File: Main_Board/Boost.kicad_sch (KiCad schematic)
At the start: 13 parts, among them U3 TLV61070ADBV

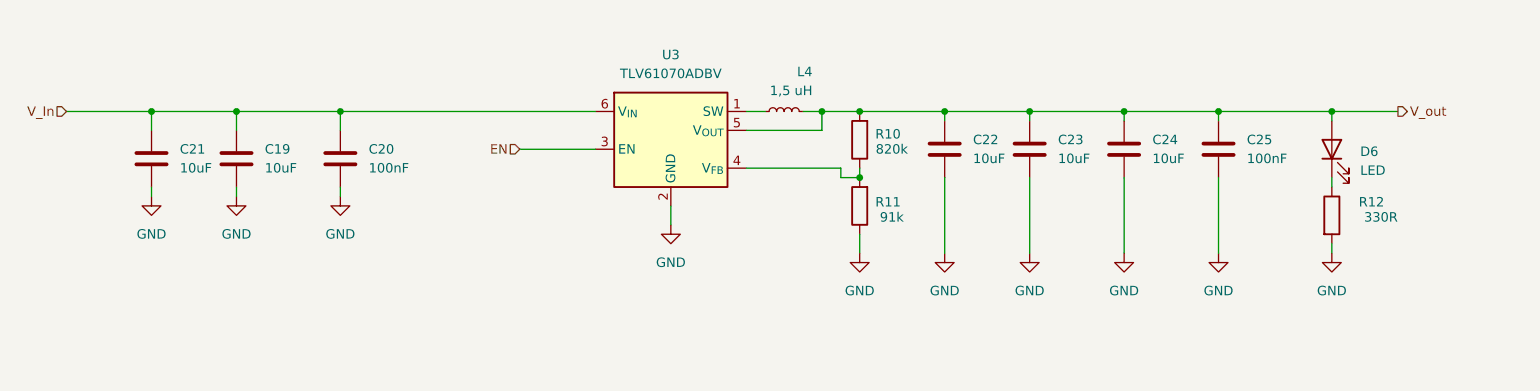
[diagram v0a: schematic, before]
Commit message: Input Protection
Irlm is left to be calculated
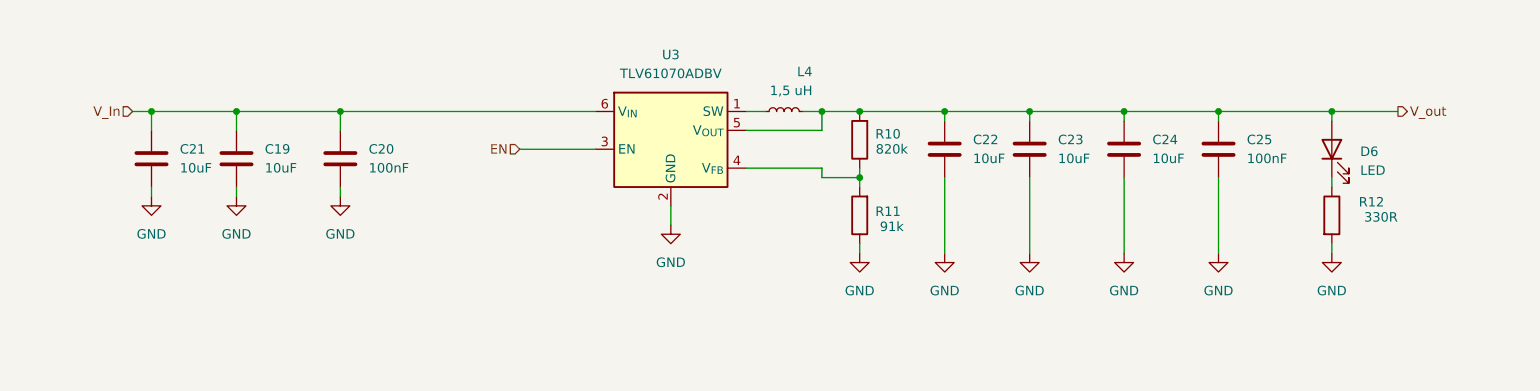
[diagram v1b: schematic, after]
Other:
- moved on the sheet: R11
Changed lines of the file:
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@@
 	(wire
 		(pts
-			(xy 134.62 93.98) (xy 147.32 93.98)
-		)
-		(stroke
-			(width 0)
-			(type default)
-		)
-	)
-	(wire
-		(pts
-			(xy 149.86 102.87) (xy 149.86 105.41)
+			(xy 134.62 93.98) (xy 144.78 93.98)
+		)
+		(stroke
+			(width 0)
+			(type default)
+		)
+	)
+	(wire
+		(pts
+			(xy 149.86 104.14) (xy 149.86 105.41)
 		)
 		(stroke
@@
 	(wire
 		(pts
+			(xy 149.86 96.52) (xy 149.86 95.25)
+		)
+		(stroke
+			(width 0)
+			(type default)
+		)
+	)
+	(wire
+		(pts
 			(xy 161.29 87.63) (xy 161.29 86.36)
 		)
@@
 	(wire
 		(pts
-			(xy 43.18 86.36) (xy 54.61 86.36)
+			(xy 52.07 86.36) (xy 54.61 86.36)
 		)
 		(stroke
@@
 	(wire
 		(pts
-			(xy 147.32 93.98) (xy 147.32 95.25)
+			(xy 144.78 93.98) (xy 144.78 95.25)
 		)
 		(stroke
@@
 	(wire
 		(pts
-			(xy 147.32 95.25) (xy 149.86 95.25)
+			(xy 144.78 95.25) (xy 149.86 95.25)
 		)
 		(stroke
@@
 		)
 	)
-	(hierarchical_label "V_In"
+	(hierarchical_label "EN"
 		(shape input)
-		(at 43.18 86.36 180)
+		(at 104.14 91.44 180)
 		(effects
 			(font
@@
 		)
 	)
-	(hierarchical_label "EN"
+	(hierarchical_label "V_In"
 		(shape input)
-		(at 104.14 91.44 180)
+		(at 52.07 86.36 180)
 		(effects
 			(font
@@
 	(symbol
 		(lib_id "Device:R")
-		(at 149.86 99.06 180)
+		(at 149.86 100.33 180)
 		(unit 1)
 		(body_style 1)
@@
 		(dnp no)
 		(property "Reference" "R11"
-			(at 153.67 98.552 0)
+			(at 153.67 99.822 0)
 			(show_name no)
 			(do_not_autoplace no)
@@
 		)
 		(property "Value" "91k"
-			(at 154.178 100.584 0)
+			(at 154.178 101.854 0)
 			(show_name no)
 			(do_not_autoplace no)
@@
 		)
 		(property "Footprint" ""
-			(at 151.638 99.06 90)
+			(at 151.638 100.33 90)
 			(hide yes)
 			(show_name no)
@@
 		)
 		(property "Datasheet" ""
-			(at 149.86 99.06 0)
+			(at 149.86 100.33 0)
 			(hide yes)
 			(show_name no)
@@
 		)
 		(property "Description" "Resistor"
-			(at 149.86 99.06 0)
-			(hide yes)
-			(show_name no)
+			(at 149.86 100.33 0)
+			(hide yes)
+			(show_name no)

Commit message: Add buzzer, Add LED, ADD R&D jumper
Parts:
- renumbered C21 to C20, C19 to C21, C20 to C22, C22 to C23, C23 to C24, C24 to C25, C25 to C26, L4 to L3, R10 to R25, R11 to R26, R12 to R27, U3 to U5
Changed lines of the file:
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@@
 		(dnp no)
 		(fields_autoplaced yes)
-		(property "Reference" "#PWR052"
+		(property "Reference" "#PWR055"
 			(at 149.86 111.76 0)
 			(hide yes)
@@
 			(project "Main_Board"
 				(path "/7481738f-7c20-40bb-99b0-6ccd4168db33/4704f5be-58a0-4191-b01f-84980581c4a3/0e0beba8-65f6-4fdb-a51c-805313830f65"
-					(reference "#PWR052")
+					(reference "#PWR055")
 					(unit 1)
 				)
@@
 		(in_pos_files yes)
 		(dnp no)
-		(property "Reference" "R11"
+		(property "Reference" "R26"
 			(at 153.67 99.822 0)
 			(show_name no)
@@
 			(project "Main_Board"
 				(path "/7481738f-7c20-40bb-99b0-6ccd4168db33/4704f5be-58a0-4191-b01f-84980581c4a3/0e0beba8-65f6-4fdb-a51c-805313830f65"
-					(reference "R11")
+					(reference "R26")
 					(unit 1)
 				)
@@
 		(dnp no)
 		(fields_autoplaced yes)
-		(property "Reference" "#PWR053"
+		(property "Reference" "#PWR060"
 			(at 213.36 111.76 0)
 			(hide yes)
@@
 			(project "Main_Board"
 				(path "/7481738f-7c20-40bb-99b0-6ccd4168db33/4704f5be-58a0-4191-b01f-84980581c4a3/0e0beba8-65f6-4fdb-a51c-805313830f65"
-					(reference "#PWR053")
+					(reference "#PWR060")
 					(unit 1)
 				)
@@
 		(dnp no)
 		(fields_autoplaced yes)
-		(property "Reference" "C20"
+		(property "Reference" "C22"
 			(at 83.82 91.4399 0)
 			(show_name no)
@@
 			(project "Main_Board"
 				(path "/7481738f-7c20-40bb-99b0-6ccd4168db33/4704f5be-58a0-4191-b01f-84980581c4a3/0e0beba8-65f6-4fdb-a51c-805313830f65"
-					(reference "C20")
+					(reference "C22")
 					(unit 1)
 				)
@@
 		(dnp no)
 		(fields_autoplaced yes)
-		(property "Reference" "U3"
+		(property "Reference" "U5"
 			(at 124.46 78.74 0)
 			(show_name no)
@@
 			(project "Main_Board"
 				(path "/7481738f-7c20-40bb-99b0-6ccd4168db33/4704f5be-58a0-4191-b01f-84980581c4a3/0e0beba8-65f6-4fdb-a51c-805313830f65"
-					(reference "U3")
+					(reference "U5")
 					(unit 1)
 				)
@@
 		(dnp no)
 		(fields_autoplaced yes)
-		(property "Reference" "C22"
+		(property "Reference" "C23"
 			(at 165.1 90.1699 0)
 			(show_name no)
@@
 			(project "Main_Board"
 				(path "/7481738f-7c20-40bb-99b0-6ccd4168db33/4704f5be-58a0-4191-b01f-84980581c4a3/0e0beba8-65f6-4fdb-a51c-805313830f65"
-					(reference "C22")
+					(reference "C23")
 					(unit 1)
 				)
@@
 		(in_pos_files yes)
 		(dnp no)
-		(property "Reference" "L4"
+		(property "Reference" "L3"
 			(at 143.51 81.026 90)
 			(show_name no)
@@
 			(project "Main_Board"
 				(path "/7481738f-7c20-40bb-99b0-6ccd4168db33/4704f5be-58a0-4191-b01f-84980581c4a3/0e0beba8-65f6-4fdb-a51c-805313830f65"
-					(reference "L4")
+					(reference "L3")
 					(unit 1)
 				)
@@
 		(dnp no)
 		(fields_autoplaced yes)
-		(property "Reference" "#PWR048"
+		(property "Reference" "#PWR056"
 			(at 161.29 111.76 0)
 			(hide yes)
@@
 			(project "Main_Board"
 				(path "/7481738f-7c20-40bb-99b0-6ccd4168db33/4704f5be-58a0-4191-b01f-84980581c4a3/0e0beba8-65f6-4fdb-a51c-805313830f65"
-					(reference "#PWR048")
+					(reference "#PWR056")
 					(unit 1)
 				)
@@
 		(dnp no)
 		(fields_autoplaced yes)
-		(property "Reference" "#PWR044"
+		(property "Reference" "#PWR052"
 			(at 66.04 104.14 0)
 			(hide yes)
@@
 			(project "Main_Board"
 				(path "/7481738f-7c20-40bb-99b0-6ccd4168db33/4704f5be-58a0-4191-b01f-84980581c4a3/0e0beba8-65f6-4fdb-a51c-805313830f65"
-					(reference "#PWR044")
+					(reference "#PWR052")
 					(unit 1)
 				)
@@
 		(dnp no)
 		(fields_autoplaced yes)
-		(property "Reference" "C25"
+		(property "Reference" "C26"
 			(at 201.93 90.1699 0)
 			(show_name no)
@@
 			(project "Main_Board"
 				(path "/7481738f-7c20-40bb-99b0-6ccd4168db33/4704f5be-58a0-4191-b01f-84980581c4a3/0e0beba8-65f6-4fdb-a51c-805313830f65"
-					(reference "C25")
+					(reference "C26")
 					(unit 1)
 				)
@@
 		(dnp no)
 		(fields_autoplaced yes)
-		(property "Reference" "C21"
+		(property "Reference" "C20"
 			(at 58.42 91.4399 0)
 			(show_name no)
@@
 			(project "Main_Board"
 				(path "/7481738f-7c20-40bb-99b0-6ccd4168db33/4704f5be-58a0-4191-b01f-84980581c4a3/0e0beba8-65f6-4fdb-a51c-805313830f65"
-					(reference "C21")
+					(reference "C20")
 					(unit 1)
 				)
@@
 		(dnp no)
 		(fields_autoplaced yes)
-		(property "Reference" "#PWR047"
+		(property "Reference" "#PWR054"
 			(at 124.46 107.95 0)
 			(hide yes)
@@
 			(project "Main_Board"
 				(path "/7481738f-7c20-40bb-99b0-6ccd4168db33/4704f5be-58a0-4191-b01f-84980581c4a3/0e0beba8-65f6-4fdb-a51c-805313830f65"
-					(reference "#PWR047")
+					(reference "#PWR054")
 					(unit 1)
 				)
@@
 		(dnp no)
 		(fields_autoplaced yes)
-		(property "Reference" "#PWR049"
+		(property "Reference" "#PWR057"
 			(at 172.72 111.76 0)
 			(hide yes)
@@
 			(project "Main_Board"
 				(path "/7481738f-7c20-40bb-99b0-6ccd4168db33/4704f5be-58a0-4191-b01f-84980581c4a3/0e0beba8-65f6-4fdb-a51c-805313830f65"
-					(reference "#PWR049")
+					(reference "#PWR057")
 					(unit 1)
 				)
@@
 		(dnp no)
 		(fields_autoplaced yes)
-		(property "Reference" "#PWR045"
+		(property "Reference" "#PWR053"
 			(at 80.01 104.14 0)
 			(hide yes)
@@
 			(project "Main_Board"
 				(path "/7481738f-7c20-40bb-99b0-6ccd4168db33/4704f5be-58a0-4191-b01f-84980581c4a3/0e0beba8-65f6-4fdb-a51c-805313830f65"
-					(reference "#PWR045")
+					(reference "#PWR053")
 					(unit 1)
 				)
@@
 		(dnp no)
 		(fields_autoplaced yes)
-		(property "Reference" "C19"
+		(property "Reference" "C21"
 			(at 69.85 91.4399 0)
 			(show_name no)
@@
 			(project "Main_Board"
 				(path "/7481738f-7c20-40bb-99b0-6ccd4168db33/4704f5be-58a0-4191-b01f-84980581c4a3/0e0beba8-65f6-4fdb-a51c-805313830f65"
-					(reference "C19")
+					(reference "C21")
 					(unit 1)
 				)
@@
 		(dnp no)
 		(fields_autoplaced yes)
-		(property "Reference" "#PWR046"
+		(property "Reference" "#PWR051"
 			(at 54.61 104.14 0)
 			(hide yes)
@@
 			(project "Main_Board"
 				(path "/7481738f-7c20-40bb-99b0-6ccd4168db33/4704f5be-58a0-4191-b01f-84980581c4a3/0e0beba8-65f6-4fdb-a51c-805313830f65"
-					(reference "#PWR046")
+					(reference "#PWR051")
 					(unit 1)
 				)
@@
 		(dnp no)
 		(fields_autoplaced yes)
-		(property "Reference" "#PWR050"
+		(property "Reference" "#PWR058"
 			(at 185.42 111.76 0)
 			(hide yes)
@@
 			(project "Main_Board"
 				(path "/7481738f-7c20-40bb-99b0-6ccd4168db33/4704f5be-58a0-4191-b01f-84980581c4a3/0e0beba8-65f6-4fdb-a51c-805313830f65"
-					(reference "#PWR050")
+					(reference "#PWR058")
 					(unit 1)
 				)
@@
 		(dnp no)
 		(fields_autoplaced yes)
-		(property "Reference" "C23"
+		(property "Reference" "C24"
 			(at 176.53 90.1699 0)
 			(show_name no)
@@
 			(project "Main_Board"
 				(path "/7481738f-7c20-40bb-99b0-6ccd4168db33/4704f5be-58a0-4191-b01f-84980581c4a3/0e0beba8-65f6-4fdb-a51c-805313830f65"
-					(reference "C23")
+					(reference "C24")
 					(unit 1)
 				)
@@
 		(dnp no)
 		(fields_autoplaced yes)
-		(property "Reference" "#PWR051"
+		(property "Reference" "#PWR059"
 			(at 198.12 111.76 0)
 			(hide yes)
@@
 			(project "Main_Board"
 				(path "/7481738f-7c20-40bb-99b0-6ccd4168db33/4704f5be-58a0-4191-b01f-84980581c4a3/0e0beba8-65f6-4fdb-a51c-805313830f65"
-					(reference "#PWR051")
+					(reference "#PWR059")
 					(unit 1)
 				)
@@
 		(in_pos_files yes)
 		(dnp no)
-		(property "Reference" "R12"
+		(property "Reference" "R27"
 			(at 218.694 98.552 0)
 			(show_name no)
@@
 			(project "Main_Board"
 				(path "/7481738f-7c20-40bb-99b0-6ccd4168db33/4704f5be-58a0-4191-b01f-84980581c4a3/0e0beba8-65f6-4fdb-a51c-805313830f65"
-					(reference "R12")
+					(reference "R27")
 					(unit 1)
 				)
@@
 		(dnp no)
 		(fields_autoplaced yes)
-		(property "Reference" "C24"
+		(property "Reference" "C25"
 			(at 189.23 90.1699 0)
 			(show_name no)
@@
 			(project "Main_Board"
 				(path "/7481738f-7c20-40bb-99b0-6ccd4168db33/4704f5be-58a0-4191-b01f-84980581c4a3/0e0beba8-65f6-4fdb-a51c-805313830f65"
-					(reference "C24")
+					(reference "C25")
 					(unit 1)
 				)
@@
 		(in_pos_files yes)
 		(dnp no)
-		(property "Reference" "R10"
+		(property "Reference" "R25"
 			(at 153.67 89.408 0)
 			(show_name no)
@@
 			(project "Main_Board"
 				(path "/7481738f-7c20-40bb-99b0-6ccd4168db33/4704f5be-58a0-4191-b01f-84980581c4a3/0e0beba8-65f6-4fdb-a51c-805313830f65"
-					(reference "R10")
-					(unit 1)
-				)
+					(reference "R25")
+					(unit 1)
+				)

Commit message: ADD footprints
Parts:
- C20, C21, C22, C23, C24, C25, C26: footprint (none) -> Capacitor_SMD:C_0603_1608Metric
- D6: footprint (none) -> Diode_SMD:D_0603_1608Metric
- L3: footprint (none) -> Inductor_SMD:L_Taiyo-Yuden_MD-3030; PN (none) -> LQH3NPN1R5MJRL
- R25, R26, R27: footprint (none) -> Resistor_SMD:R_0603_1608Metric
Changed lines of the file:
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@@
 			)
 		)
-		(property "Footprint" ""
+		(property "Footprint" "Resistor_SMD:R_0603_1608Metric"
 			(at 151.638 100.33 90)
 			(hide yes)
@@
 			)
 		)
-		(property "Footprint" ""
+		(property "Footprint" "Capacitor_SMD:C_0603_1608Metric"
 			(at 80.9752 96.52 0)
 			(hide yes)
@@
 			)
 		)
-		(property "Footprint" ""
+		(property "Footprint" "Capacitor_SMD:C_0603_1608Metric"
 			(at 162.2552 95.25 0)
 			(hide yes)
@@
 			)
 		)
-		(property "Footprint" ""
+		(property "Footprint" "Inductor_SMD:L_Taiyo-Yuden_MD-3030"
 			(at 139.7 86.36 0)
 			(hide yes)
@@
 			)
 		)
-		(property "Datasheet" ""
+		(property "Datasheet" "LQH3NPN1R5MJRL"
 			(at 139.7 86.36 0)
 			(hide yes)
@@
 			)
 		)
+		(property "PN" "LQH3NPN1R5MJRL"
+			(at 139.7 86.36 90)
+			(hide yes)
+			(show_name no)
+			(do_not_autoplace no)
+			(effects
+				(font
+					(size 1.27 1.27)
+				)
+			)
+		)
 		(pin "2"
 		)
@@
 			)
 		)
-		(property "Footprint" ""
+		(property "Footprint" "Capacitor_SMD:C_0603_1608Metric"
 			(at 199.0852 95.25 0)
 			(hide yes)
@@
 			)
 		)
-		(property "Footprint" ""
+		(property "Footprint" "Capacitor_SMD:C_0603_1608Metric"
 			(at 55.5752 96.52 0)
 			(hide yes)
@@
 			)
 		)
-		(property "Footprint" ""
+		(property "Footprint" "Diode_SMD:D_0603_1608Metric"
 			(at 213.36 91.44 0)
 			(hide yes)
@@
 			)
 		)
-		(property "Footprint" ""
+		(property "Footprint" "Capacitor_SMD:C_0603_1608Metric"
 			(at 67.0052 96.52 0)
 			(hide yes)
@@
 			)
 		)
-		(property "Footprint" ""
+		(property "Footprint" "Capacitor_SMD:C_0603_1608Metric"
 			(at 173.6852 95.25 0)
 			(hide yes)
@@
 			)
 		)
-		(property "Footprint" ""
+		(property "Footprint" "Resistor_SMD:R_0603_1608Metric"
 			(at 211.582 100.33 90)
 			(hide yes)
@@
 			)
 		)
-		(property "Footprint" ""
+		(property "Footprint" "Capacitor_SMD:C_0603_1608Metric"
 			(at 186.3852 95.25 0)
 			(hide yes)
@@
 			)
 		)
-		(property "Footprint" ""
+		(property "Footprint" "Resistor_SMD:R_0603_1608Metric"
 			(at 151.638 90.17 90)
 			(hide yes)

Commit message: Add pyro channels x2
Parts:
- renumbered R25 to R27, R26 to R28, R27 to R29
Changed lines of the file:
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@@
 		(dnp no)
 		(fields_autoplaced yes)
-		(property "Reference" "#PWR055"
+		(property "Reference" "#PWR059"
 			(at 149.86 111.76 0)
 			(hide yes)
@@
 			(project "Main_Board"
 				(path "/7481738f-7c20-40bb-99b0-6ccd4168db33/4704f5be-58a0-4191-b01f-84980581c4a3/0e0beba8-65f6-4fdb-a51c-805313830f65"
-					(reference "#PWR055")
+					(reference "#PWR059")
 					(unit 1)
 				)
@@
 		(in_pos_files yes)
 		(dnp no)
-		(property "Reference" "R26"
+		(property "Reference" "R28"
 			(at 153.67 99.822 0)
 			(show_name no)
@@
 			(project "Main_Board"
 				(path "/7481738f-7c20-40bb-99b0-6ccd4168db33/4704f5be-58a0-4191-b01f-84980581c4a3/0e0beba8-65f6-4fdb-a51c-805313830f65"
-					(reference "R26")
+					(reference "R28")
 					(unit 1)
 				)
@@
 		(dnp no)
 		(fields_autoplaced yes)
-		(property "Reference" "#PWR060"
+		(property "Reference" "#PWR064"
 			(at 213.36 111.76 0)
 			(hide yes)
@@
 			(project "Main_Board"
 				(path "/7481738f-7c20-40bb-99b0-6ccd4168db33/4704f5be-58a0-4191-b01f-84980581c4a3/0e0beba8-65f6-4fdb-a51c-805313830f65"
-					(reference "#PWR060")
+					(reference "#PWR064")
 					(unit 1)
 				)
@@
 		(dnp no)
 		(fields_autoplaced yes)
-		(property "Reference" "#PWR056"
+		(property "Reference" "#PWR060"
 			(at 161.29 111.76 0)
 			(hide yes)
@@
 			(project "Main_Board"
 				(path "/7481738f-7c20-40bb-99b0-6ccd4168db33/4704f5be-58a0-4191-b01f-84980581c4a3/0e0beba8-65f6-4fdb-a51c-805313830f65"
-					(reference "#PWR056")
+					(reference "#PWR060")
 					(unit 1)
 				)
@@
 		(dnp no)
 		(fields_autoplaced yes)
-		(property "Reference" "#PWR052"
+		(property "Reference" "#PWR056"
 			(at 66.04 104.14 0)
 			(hide yes)
@@
 			(project "Main_Board"
 				(path "/7481738f-7c20-40bb-99b0-6ccd4168db33/4704f5be-58a0-4191-b01f-84980581c4a3/0e0beba8-65f6-4fdb-a51c-805313830f65"
-					(reference "#PWR052")
+					(reference "#PWR056")
 					(unit 1)
 				)
@@
 		(dnp no)
 		(fields_autoplaced yes)
-		(property "Reference" "#PWR054"
+		(property "Reference" "#PWR058"
 			(at 124.46 107.95 0)
 			(hide yes)
@@
 			(project "Main_Board"
 				(path "/7481738f-7c20-40bb-99b0-6ccd4168db33/4704f5be-58a0-4191-b01f-84980581c4a3/0e0beba8-65f6-4fdb-a51c-805313830f65"
-					(reference "#PWR054")
+					(reference "#PWR058")
 					(unit 1)
 				)
@@
 		(dnp no)
 		(fields_autoplaced yes)
-		(property "Reference" "#PWR057"
+		(property "Reference" "#PWR061"
 			(at 172.72 111.76 0)
 			(hide yes)
@@
 			(project "Main_Board"
 				(path "/7481738f-7c20-40bb-99b0-6ccd4168db33/4704f5be-58a0-4191-b01f-84980581c4a3/0e0beba8-65f6-4fdb-a51c-805313830f65"
-					(reference "#PWR057")
+					(reference "#PWR061")
 					(unit 1)
 				)
@@
 		(dnp no)
 		(fields_autoplaced yes)
-		(property "Reference" "#PWR053"
+		(property "Reference" "#PWR057"
 			(at 80.01 104.14 0)
 			(hide yes)
@@
 			(project "Main_Board"
 				(path "/7481738f-7c20-40bb-99b0-6ccd4168db33/4704f5be-58a0-4191-b01f-84980581c4a3/0e0beba8-65f6-4fdb-a51c-805313830f65"
-					(reference "#PWR053")
+					(reference "#PWR057")
 					(unit 1)
 				)
@@
 		(dnp no)
 		(fields_autoplaced yes)
-		(property "Reference" "#PWR051"
+		(property "Reference" "#PWR055"
 			(at 54.61 104.14 0)
 			(hide yes)
@@
 			(project "Main_Board"
 				(path "/7481738f-7c20-40bb-99b0-6ccd4168db33/4704f5be-58a0-4191-b01f-84980581c4a3/0e0beba8-65f6-4fdb-a51c-805313830f65"
-					(reference "#PWR051")
+					(reference "#PWR055")
 					(unit 1)
 				)
@@
 		(dnp no)
 		(fields_autoplaced yes)
-		(property "Reference" "#PWR058"
+		(property "Reference" "#PWR062"
 			(at 185.42 111.76 0)
 			(hide yes)
@@
 			(project "Main_Board"
 				(path "/7481738f-7c20-40bb-99b0-6ccd4168db33/4704f5be-58a0-4191-b01f-84980581c4a3/0e0beba8-65f6-4fdb-a51c-805313830f65"
-					(reference "#PWR058")
+					(reference "#PWR062")
 					(unit 1)
 				)
@@
 		(dnp no)
 		(fields_autoplaced yes)
-		(property "Reference" "#PWR059"
+		(property "Reference" "#PWR063"
 			(at 198.12 111.76 0)
 			(hide yes)
@@
 			(project "Main_Board"
 				(path "/7481738f-7c20-40bb-99b0-6ccd4168db33/4704f5be-58a0-4191-b01f-84980581c4a3/0e0beba8-65f6-4fdb-a51c-805313830f65"
-					(reference "#PWR059")
+					(reference "#PWR063")
 					(unit 1)
 				)
@@
 		(in_pos_files yes)
 		(dnp no)
-		(property "Reference" "R27"
+		(property "Reference" "R29"
 			(at 218.694 98.552 0)
 			(show_name no)
@@
 			(project "Main_Board"
 				(path "/7481738f-7c20-40bb-99b0-6ccd4168db33/4704f5be-58a0-4191-b01f-84980581c4a3/0e0beba8-65f6-4fdb-a51c-805313830f65"
-					(reference "R27")
+					(reference "R29")
 					(unit 1)
 				)
@@
 		(in_pos_files yes)
 		(dnp no)
-		(property "Reference" "R25"
+		(property "Reference" "R27"
 			(at 153.67 89.408 0)
 			(show_name no)
@@
 			(project "Main_Board"
 				(path "/7481738f-7c20-40bb-99b0-6ccd4168db33/4704f5be-58a0-4191-b01f-84980581c4a3/0e0beba8-65f6-4fdb-a51c-805313830f65"
-					(reference "R25")
-					(unit 1)
-				)
+					(reference "R27")
+					(unit 1)
+				)

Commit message: Fix schematic readibility
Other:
- moved on the sheet: C20, C21, C22, C23, C24, C25, C26, D6, L3, R27, R28, R29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

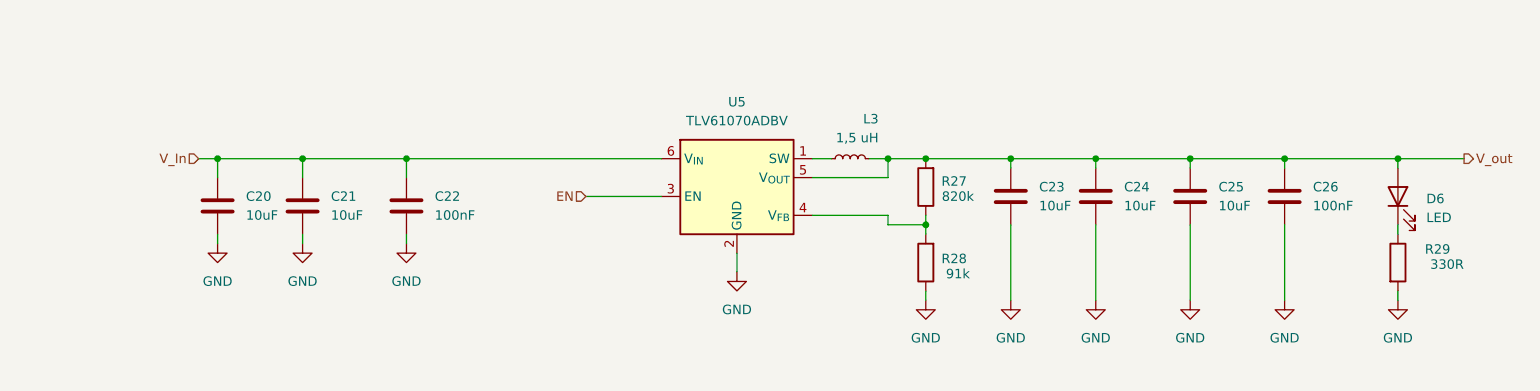
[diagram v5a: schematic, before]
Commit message: Standardise resistor value mark for BOM + pyro footprints
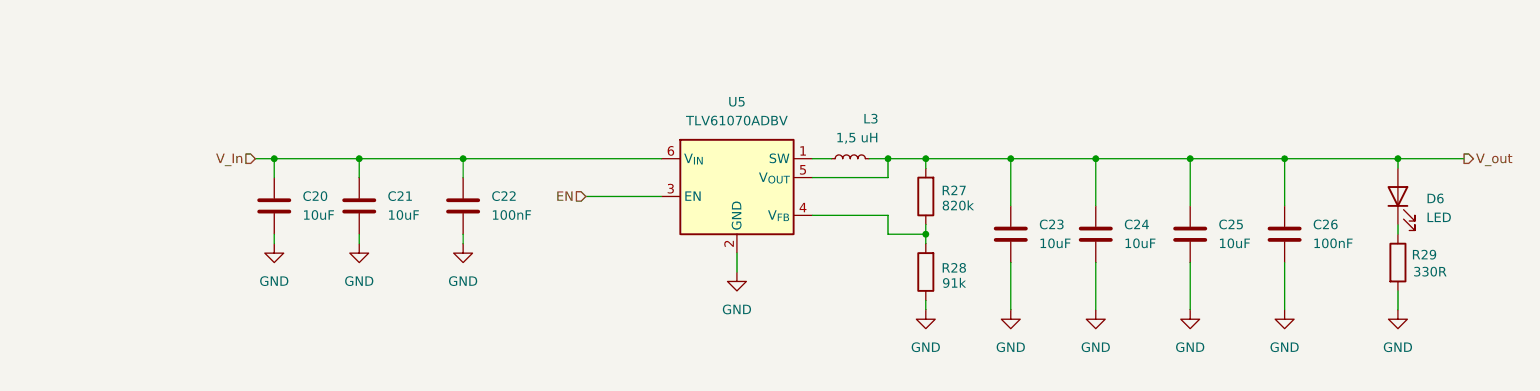
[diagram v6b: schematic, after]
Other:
- moved on the sheet: C20, C21, C22, C23, C24, C25, C26, R27, R28
